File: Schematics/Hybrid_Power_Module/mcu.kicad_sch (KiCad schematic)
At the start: 36 parts, among them J5 USB_C_Female_USB2_Small, J6 SWD_B, SW1 SW_STM_RESET, SW2 SW_STM_BOOT_MODE, U13 CP2102N-A02-GQFN20R, U14 STM32F103CBT6, U15 TCAN1051HGVDR, U16 BY25Q128ES, Y1 X322516MMB4SI

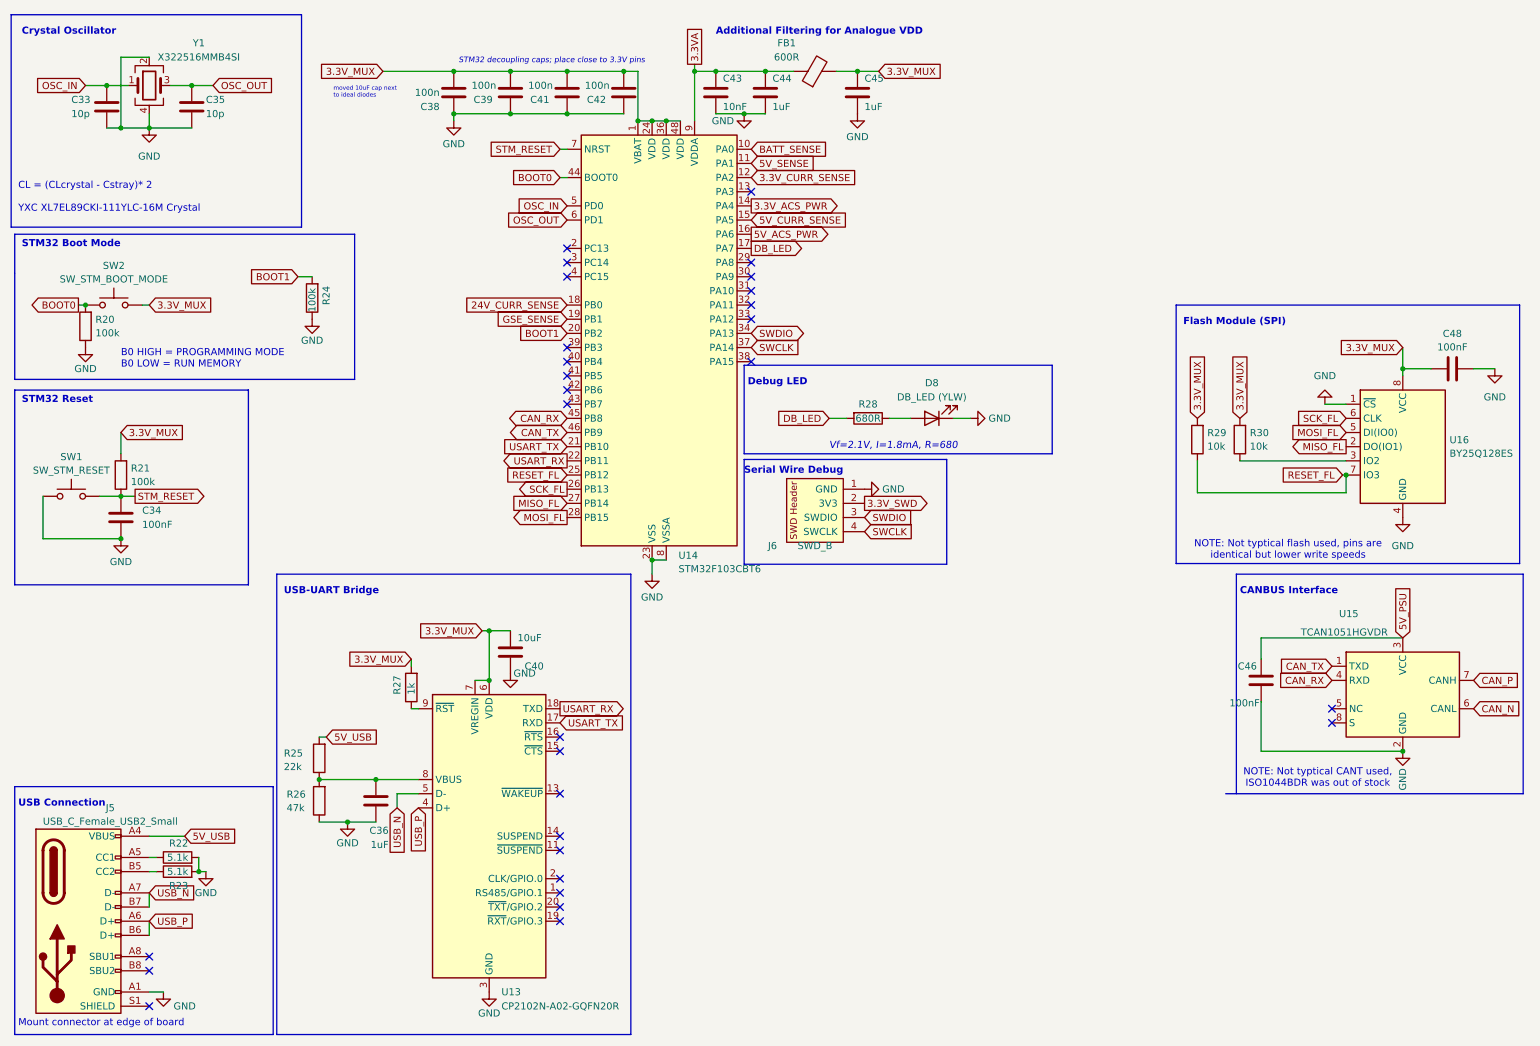
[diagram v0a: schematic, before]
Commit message: fix: Updates after testing, for next revision
 - add current limiting to GSE RPP zener shunt
 - switched 5v current sensor
 - flipped CAN and UART polarity
 - add 3.3v reference to CAN transceiver
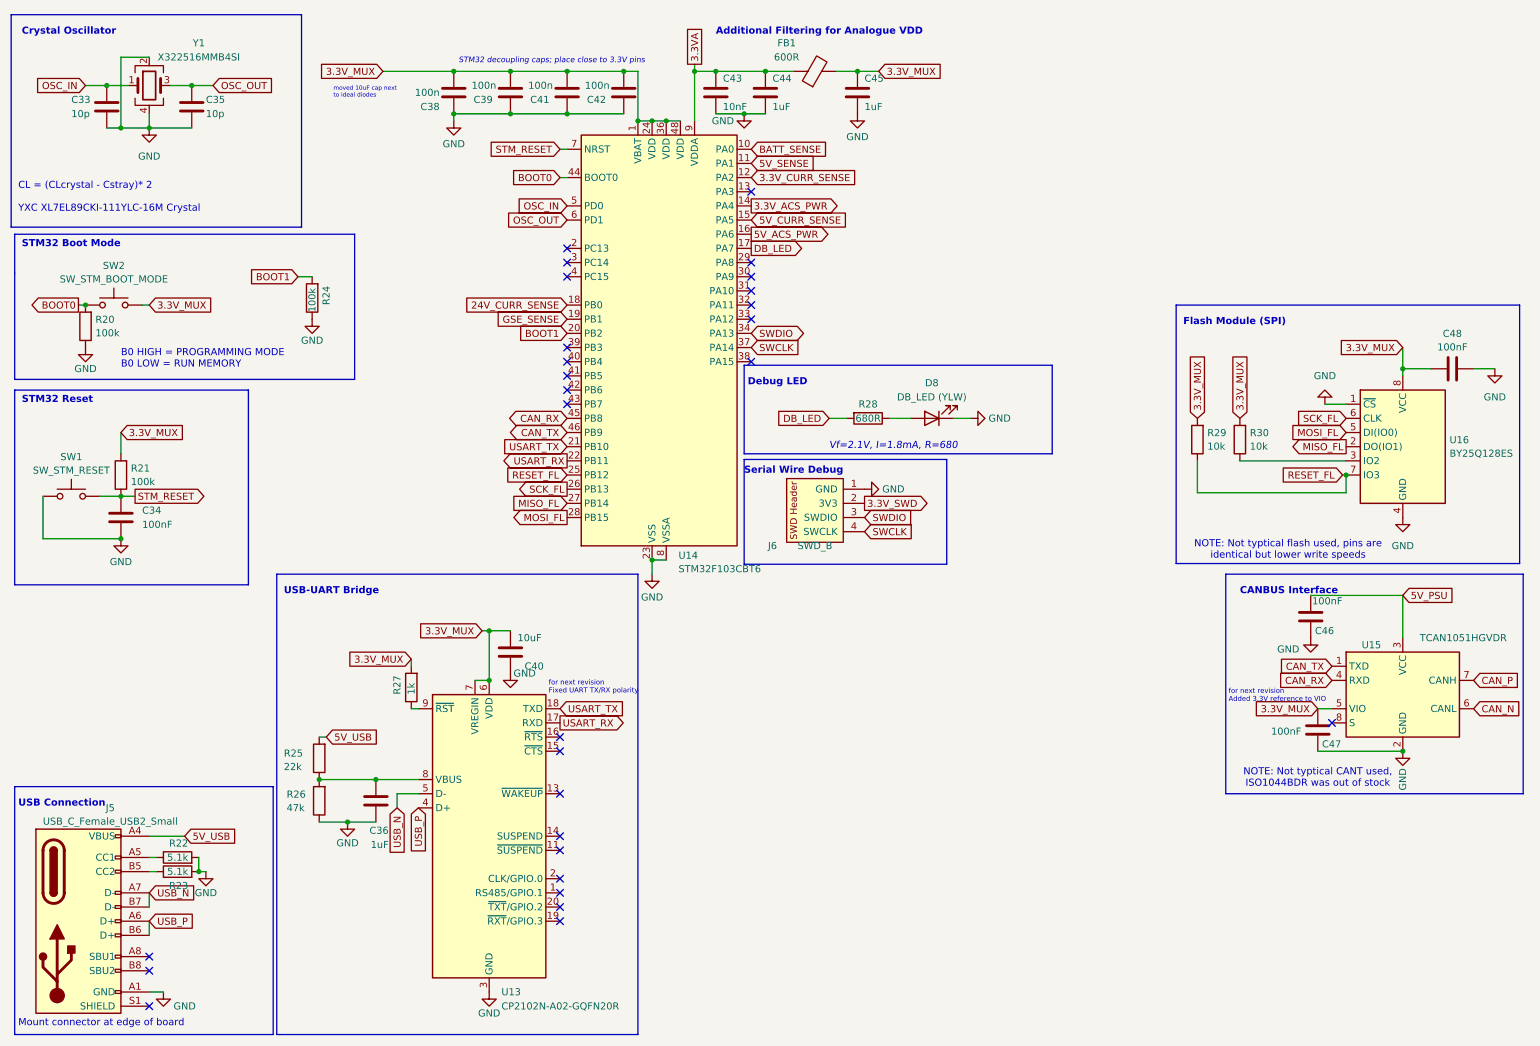
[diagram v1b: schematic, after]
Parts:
- added C47: 100nF, Capacitor_SMD:C_0603_1608Metric, symbol Device:C
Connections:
- net 3.3V_MUX: now also U15.5 (VIO), C47.1
- net 5V_PSU: now also C46.1; no longer C46.2
- net GND: now also C46.2, C47.2; no longer C46.1
- net USART_RX: now also U13.17 (RXD); no longer U13.18 (TXD)
- net USART_TX: now also U13.18 (TXD); no longer U13.17 (RXD)
- no-connect marks 29 -> 28
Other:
- note added: "for next revision Added 3.3V reference to VIO"
- note added: "for next revision Fixed UART TX/RX polarity"
- moved on the sheet: C46
